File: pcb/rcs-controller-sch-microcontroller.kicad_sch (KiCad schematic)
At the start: 40 parts, among them J11 Conn_01x03, J4 Screw_Terminal_4_P3.50mm, J5 USB_C_Receptacle_USB2.0_14P, J6 Conn_01x03, J9 Conn_01x03, Q2 SI7465DP-T1-E3, Q3 SI7465DP-T1-E3, Q4 PMV45EN2, Q5 PMV45EN2, SW1 SW_Push, SW2 SW_Push, U1 LSM6DSOX, U4 ESP32-S3-WROOM-1

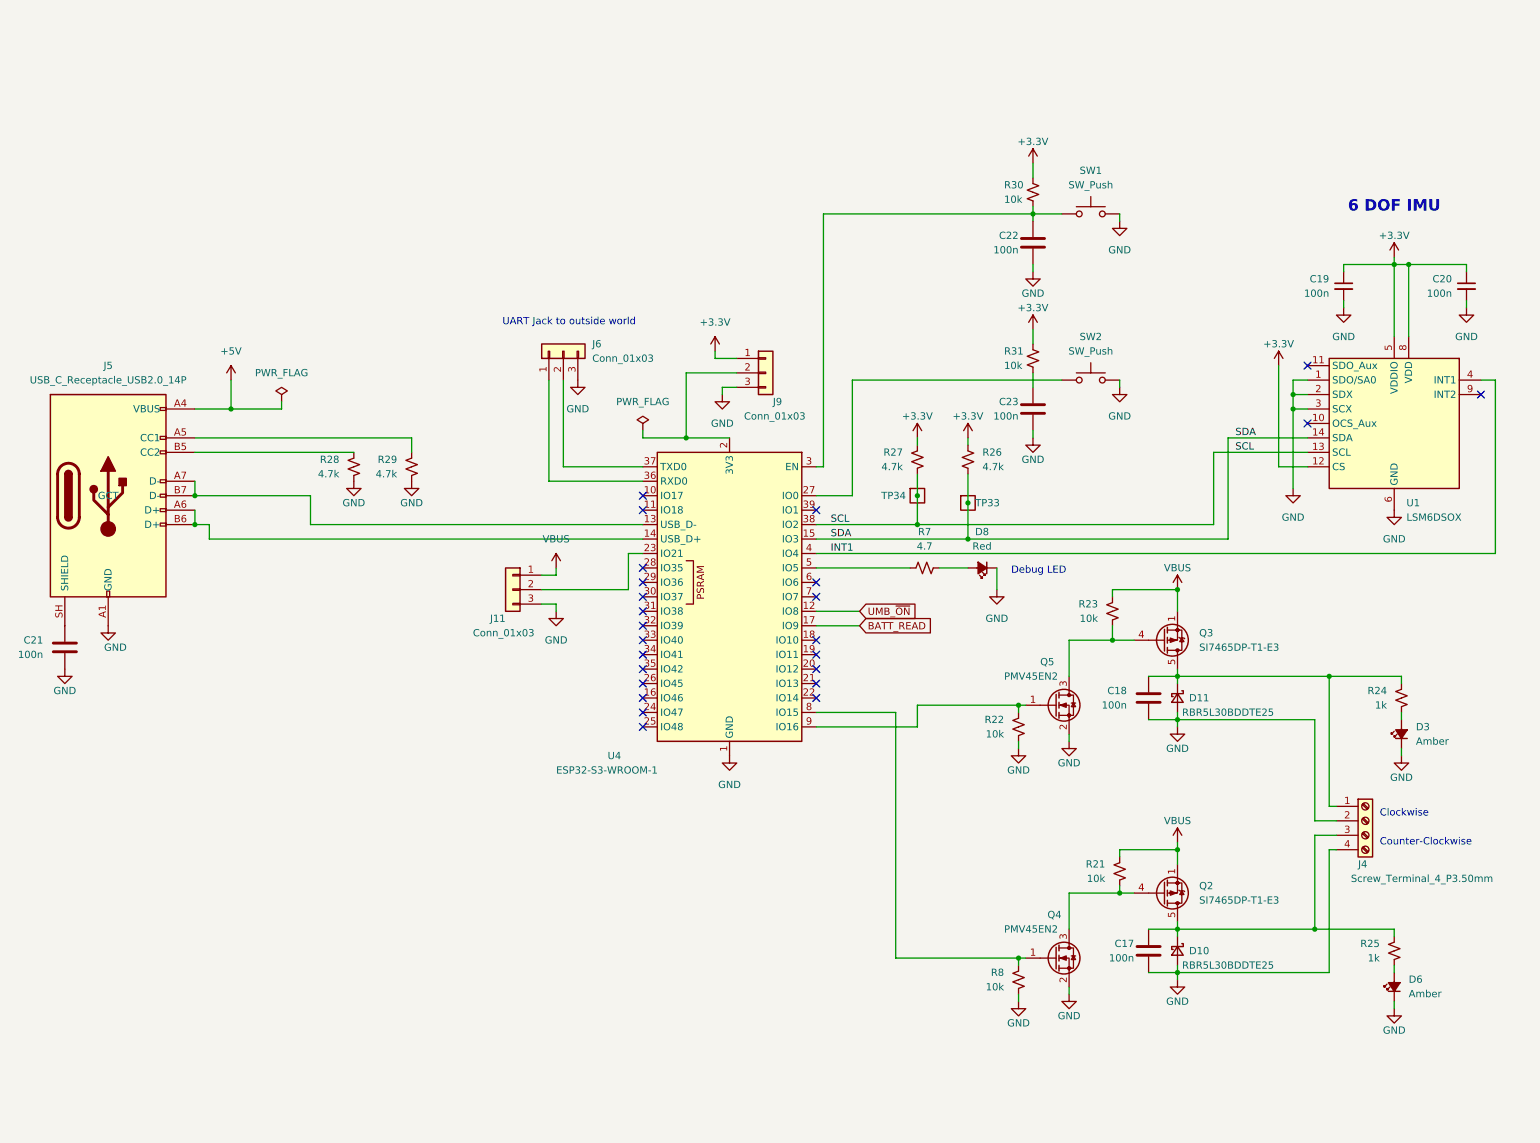
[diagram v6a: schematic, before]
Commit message: Added voltage divider for transducer and fixed connector identifier issue
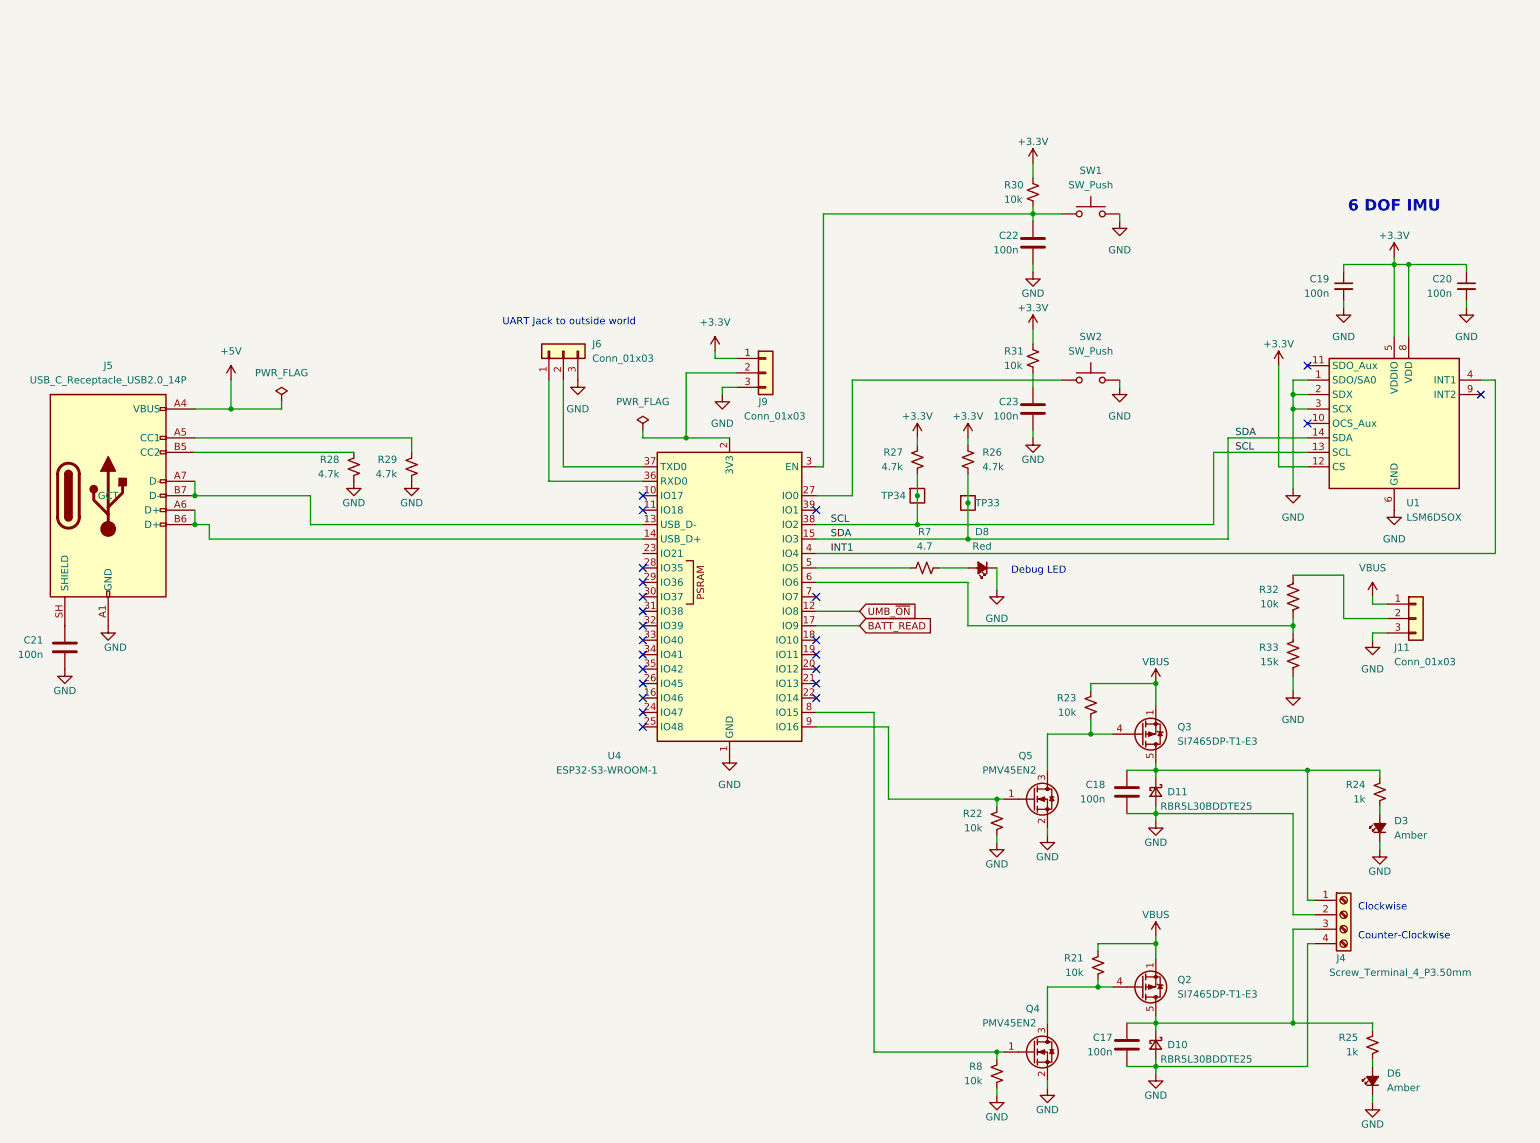
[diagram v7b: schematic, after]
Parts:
- added R32: 10k, symbol Device:R_US
- added R33: 15k, Resistor_SMD:R_0603_1608Metric, symbol Device:R_US
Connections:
- net GND: now also R33.1
- net at J11.2 (Pin_2): now also R32.1; no longer U4.23 (IO21)
- net at U4.6 (IO6): now also R32.2, R33.2
- no-connect marks 25 -> 24
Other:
- moved on the sheet: C17, C18, D10, D11, D3, D6, J11, J4, Q2, Q3, Q4, Q5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
